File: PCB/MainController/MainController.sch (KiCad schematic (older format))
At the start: 48 parts, among them J1 5V, J2 PGM, J3 SERIAL, J4 I2C, J5 IO, J6 PWR, SW1 SW_Push, SW2 SW, SW3 SW, SW4 SW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

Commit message: pcb lcd
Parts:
- added J10: Jack-DC, Connect:BARREL_JACK, symbol Jack-DC
- J1: footprint Connectors_Molex:Molex_PicoBlade_53047-0410_04x1.25mm_Straight -> Pin_Headers:Pin_Header_Straight_1x04_Pitch2.54mm
- J7, J8, J9: renamed from J?; footprint MountingHole_2.7mm_M2.5_ISO14580_Pad -> Mounting_Holes:MountingHole_2.7mm_M2.5_ISO14580_Pad
- SW2, SW3, SW4, SW5: footprint Buttons_Switches_THT:SW_PUSH_6mm -> LCD:mySW_PUSH_6mm
- SW6: footprint Buttons_Switches_THT:KSA_Tactile_SPST -> LCD:myKSA_Tactile_SPST
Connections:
- net +3V3: now also J6.3 (Pin_3), J6.4 (Pin_4)
- net +5V: now also J10.1; no longer J6.3 (Pin_3), J6.4 (Pin_4)
- net GND: now also J10.2, J10.3
- net GPA0: now also J5.8 (Pin_8); no longer J5.1 (Pin_1)
- net GPA1: now also J5.7 (Pin_7); no longer J5.2 (Pin_2)
- net GPA2: now also J5.6 (Pin_6); no longer J5.3 (Pin_3)
- net GPA3: now also J5.5 (Pin_5); no longer J5.4 (Pin_4)
- net GPA4: now also J5.4 (Pin_4); no longer J5.5 (Pin_5)
- net GPA5: now also J5.3 (Pin_3); no longer J5.6 (Pin_6)
- net GPA6: now also J5.2 (Pin_2); no longer J5.7 (Pin_7)
- net GPA7: now also J5.1 (Pin_1); no longer J5.8 (Pin_8)
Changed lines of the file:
@@
 $EndDescr
-$Comp
-L dsPIC33EPXXXGP502 U3
-U 1 1 5B13F9B3
-P 4050 4550
-F 0 "U3" H 2900 6600 50  0000 L CNN
-F 1 "dsPIC33EPXXXGP502" H 2900 6500 50  0000 L CNN
-F 2 "Housings_SOIC:SOIC-28W_7.5x17.9mm_Pitch1.27mm" H 4900 6550 50  0000 C CIN
-F 3 "" H 3350 4150 60  0000 C CNN
-	1    4050 4550
-	1    0    0    -1
-$EndComp
-$Comp
-L NHD-0216K3Z U1
-U 1 1 5B140879
-P 2300 6100
-F 0 "U1" H 2850 6350 60  0000 C CNN
-F 1 "NHD-0216K3Z" H 2300 5850 60  0000 C CNN
-F 2 "LCD:WC1602A" H 2600 5800 60  0001 C CNN
-F 3 "" H 2600 5800 60  0001 C CNN
-	1    2300 6100
-	0    -1   1    0
-$EndComp
 $Comp
 L CP C4
@@
 F 0 "J1" H 2650 1250 50  0000 C CNN
 F 1 "5V" H 2650 750 50  0000 C CNN
-F 2 "Connectors_Molex:Molex_PicoBlade_53047-0410_04x1.25mm_Straight" H 2650 1050 50  0001 C CNN
+F 2 "Pin_Headers:Pin_Header_Straight_1x04_Pitch2.54mm" H 2650 1050 50  0001 C CNN
 F 3 "" H 2650 1050 50  0001 C CNN
 	1    2650 1050
@@
 F 0 "SW6" H 9800 5860 50  0000 C CNN
 F 1 "Rotary" H 9800 5340 50  0000 C CNN
-F 2 "Buttons_Switches_THT:KSA_Tactile_SPST" H 9700 5760 50  0001 C CNN
+F 2 "LCD:myKSA_Tactile_SPST" H 9700 5760 50  0001 C CNN
 F 3 "" H 9800 5860 50  0001 C CNN
 	1    9800 5600
@@
 	2150 1250 2150 1350
 Wire Wire Line
-	1850 900  2400 900
+	1650 900  2400 900
 Connection ~ 2150 900
 Connection ~ 2150 1300
@@
 	2400 1300 2400 1150
 Wire Wire Line
-	1850 1300 2400 1300
+	1650 1300 2400 1300
 Wire Wire Line
 	2400 1150 2450 1150
@@
 F 0 "SW2" H 8800 2800 50  0000 L CNN
 F 1 "SW" H 8500 2800 50  0000 C CNN
-F 2 "Buttons_Switches_THT:SW_PUSH_6mm" H 8650 2950 50  0001 C CNN
+F 2 "LCD:mySW_PUSH_6mm" H 8650 2950 50  0001 C CNN
 F 3 "" H 8650 2950 50  0001 C CNN
 	1    8650 2750
@@
 F 0 "SW3" H 8800 2900 50  0000 L CNN
 F 1 "SW" H 8500 2900 50  0000 C CNN
-F 2 "Buttons_Switches_THT:SW_PUSH_6mm" H 8650 3050 50  0001 C CNN
+F 2 "LCD:mySW_PUSH_6mm" H 8650 3050 50  0001 C CNN
 F 3 "" H 8650 3050 50  0001 C CNN
 	1    8650 2850
@@
 F 0 "SW4" H 8800 3000 50  0000 L CNN
 F 1 "SW" H 8500 3000 50  0000 C CNN
-F 2 "Buttons_Switches_THT:SW_PUSH_6mm" H 8650 3150 50  0001 C CNN
+F 2 "LCD:mySW_PUSH_6mm" H 8650 3150 50  0001 C CNN
 F 3 "" H 8650 3150 50  0001 C CNN
 	1    8650 2950
@@
 F 0 "SW5" H 8800 3100 50  0000 L CNN
 F 1 "SW" H 8500 3100 50  0000 C CNN
-F 2 "Buttons_Switches_THT:SW_PUSH_6mm" H 8650 3250 50  0001 C CNN
+F 2 "LCD:mySW_PUSH_6mm" H 8650 3250 50  0001 C CNN
 F 3 "" H 8650 3250 50  0001 C CNN
 	1    8650 3050
@@
 L Conn_01x08 J5
 U 1 1 5B158BF5
-P 8600 3950
-F 0 "J5" H 8600 4350 50  0000 C CNN
-F 1 "IO" H 8600 3450 50  0000 C CNN
-F 2 "Connectors_Molex:Molex_PicoBlade_53047-0810_08x1.25mm_Straight" H 8600 3950 50  0001 C CNN
-F 3 "" H 8600 3950 50  0001 C CNN
-	1    8600 3950
-	1    0    0    -1
+P 8600 4050
+F 0 "J5" H 8600 4450 50  0000 C CNN
+F 1 "IO" H 8600 3550 50  0000 C CNN
+F 2 "Connectors_Molex:Molex_PicoBlade_53047-0810_08x1.25mm_Straight" H 8600 4050 50  0001 C CNN
+F 3 "" H 8600 4050 50  0001 C CNN
+	1    8600 4050
+	1    0    0    1
 $EndComp
 Wire Wire Line
@@
 	-1   0    0    1
 $EndComp
-$Comp
-L +5V #PWR038
-U 1 1 5B15A6E4
-P 9250 3600
-F 0 "#PWR038" H 9250 3450 50  0001 C CNN
-F 1 "+5V" H 9250 3740 50  0000 C CNN
-F 2 "" H 9250 3600 50  0001 C CNN
-F 3 "" H 9250 3600 50  0001 C CNN
-	1    9250 3600
-	1    0    0    -1
-$EndComp
 Wire Wire Line
 	9100 3650 9250 3650
@@
 NoConn ~ 5350 2750
 $Comp
-L Conn_01x01 J?
+L Conn_01x01 J7
 U 1 1 5B158601
 P 9900 1450
-F 0 "J?" H 9900 1550 50  0000 C CNN
+F 0 "J7" H 9900 1550 50  0000 C CNN
 F 1 "MH" H 9900 1350 50  0000 C CNN
-F 2 "MountingHole_2.7mm_M2.5_ISO14580_Pad" H 9900 1450 50  0001 C CNN
+F 2 "Mounting_Holes:MountingHole_2.7mm_M2.5_ISO14580_Pad" H 9900 1450 50  0001 C CNN
 F 3 "" H 9900 1450 50  0001 C CNN
 	1    9900 1450
@@
 $EndComp
 $Comp
-L Conn_01x01 J?
+L Conn_01x01 J8
 U 1 1 5B1587EF
 P 9900 1750
-F 0 "J?" H 9900 1850 50  0000 C CNN
+F 0 "J8" H 9900 1850 50  0000 C CNN
 F 1 "MH" H 9900 1650 50  0000 C CNN
-F 2 "MountingHole_2.7mm_M2.5_ISO14580_Pad" H 9900 1750 50  0001 C CNN
+F 2 "Mounting_Holes:MountingHole_2.7mm_M2.5_ISO14580_Pad" H 9900 1750 50  0001 C CNN
 F 3 "" H 9900 1750 50  0001 C CNN
 	1    9900 1750
@@
 $EndComp
 $Comp
-L Conn_01x01 J?
+L Conn_01x01 J9
 U 1 1 5B158894
 P 9900 2000
-F 0 "J?" H 9900 2100 50  0000 C CNN
+F 0 "J9" H 9900 2100 50  0000 C CNN
 F 1 "MH" H 9900 1900 50  0000 C CNN
-F 2 "MountingHole_2.7mm_M2.5_ISO14580_Pad" H 9900 2000 50  0001 C CNN
+F 2 "Mounting_Holes:MountingHole_2.7mm_M2.5_ISO14580_Pad" H 9900 2000 50  0001 C CNN
 F 3 "" H 9900 2000 50  0001 C CNN
 	1    9900 2000
@@
 NoConn ~ 9700 1750
 NoConn ~ 9700 2000
+$Comp
+L dsPIC33EPXXXGP502 U3
+U 1 1 5B1FC9E1
+P 4050 4550
+F 0 "U3" H 2900 6600 50  0000 L CNN
+F 1 "dsPIC33EPXXXGP502" H 2900 6500 50  0000 L CNN
+F 2 "Housings_SOIC:SOIC-28W_7.5x17.9mm_Pitch1.27mm" H 4600 6500 50  0000 C CIN
+F 3 "" H 3350 4150 60  0000 C CNN
+	1    4050 4550
+	1    0    0    -1
+$EndComp
+$Comp
+L NHD-0216K3Z U1
+U 1 1 5B1FCCB6
+P 2300 6100
+F 0 "U1" H 2850 6350 60  0000 C CNN
+F 1 "NHD-0216K3Z" H 2300 5850 60  0000 C CNN
+F 2 "LCD:WC1602A" H 2600 5800 60  0001 C CNN
+F 3 "" H 2600 5800 60  0001 C CNN
+	1    2300 6100
+	0    -1   1    0
+$EndComp
+$Comp
+L Jack-DC J10
+U 1 1 5B1FEC81
+P 1150 1100
+F 0 "J10" H 1150 1310 50  0000 C CNN
+F 1 "Jack-DC" H 1150 925 50  0000 C CNN
+F 2 "Connect:BARREL_JACK" H 1200 1060 50  0001 C CNN
+F 3 "" H 1200 1060 50  0001 C CNN
+	1    1150 1100
+	1    0    0    -1
+$EndComp
+Wire Wire Line
+	1450 1200 1650 1200
+Wire Wire Line
+	1650 1100 1650 1300
+Connection ~ 1850 1300
+Wire Wire Line
+	1450 1000 1650 1000
+Wire Wire Line
+	1650 1000 1650 900
+Connection ~ 1850 900
+Wire Wire Line
+	1450 1100 1650 1100
+Connection ~ 1650 1200
+$Comp
+L +3.3V #PWR?
+U 1 1 5B200FD1
+P 9250 3600
+F 0 "#PWR?" H 9250 3450 50  0001 C CNN
+F 1 "+3.3V" H 9250 3740 50  0000 C CNN
+F 2 "" H 9250 3600 50  0001 C CNN
+F 3 "" H 9250 3600 50  0001 C CNN
+	1    9250 3600
+	1    0    0    -1
+$EndComp
 $EndSCHEMATC

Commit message: pcb lcd
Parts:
- added D5, D6, D7: LED, LEDs:LED_0603_HandSoldering, symbol LED
- added R14, R15, R16: 2.87k, Resistors_SMD:R_0603_HandSoldering, symbol R
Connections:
- net GND: now also D5.1 (K), D6.1 (K), D7.1 (K)
- net at U3.2 (AN0/OA2OUT/RA0): now also R14.2
- net at U3.3 (AN1/C2IN1+/RA1): now also R15.2
- net at U3.4 (PGED3/V_REF_-/AN2/C2IN1-/SS1/RPI32/CTED2/RB0): now also R16.2
- new net: D5.2 (A), R16.1
- new net: D6.2 (A), R15.1
- new net: D7.2 (A), R14.1
- no-connect marks 13 -> 10
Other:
- moved on the sheet: C9, J5, J6, J9, SW2, SW3, SW4, SW5, U4

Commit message: create main pcb
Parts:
- SW6: footprint LCD:myKSA_Tactile_SPST -> Rotary-Encoders:ALPS_STEC12E08

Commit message: clean up main controller pcb
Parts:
- added J11, J12: MH, Mounting_Holes:MountingHole_2.7mm_M2.5_ISO14580_Pad, symbol Conn_01x01
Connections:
- no-connect marks 10 -> 12
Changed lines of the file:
@@
 LIBS:contrib
 LIBS:valves
+LIBS:MyLib
 LIBS:MainController-cache
 EELAYER 25 0
@@
 Wire Wire Line
 	7000 3950 7000 4050
+$Comp
+L Conn_01x01 J12
+U 1 1 5B22365B
+P 10850 1700
+F 0 "J12" H 10850 1800 50  0000 C CNN
+F 1 "MH" H 10850 1600 50  0000 C CNN
+F 2 "Mounting_Holes:MountingHole_2.7mm_M2.5_ISO14580_Pad" H 10850 1700 50  0001 C CNN
+F 3 "" H 10850 1700 50  0001 C CNN
+	1    10850 1700
+	1    0    0    -1
+$EndComp
+$Comp
+L Conn_01x01 J11
+U 1 1 5B223739
+P 10850 1400
+F 0 "J11" H 10850 1500 50  0000 C CNN
+F 1 "MH" H 10850 1300 50  0000 C CNN
+F 2 "Mounting_Holes:MountingHole_2.7mm_M2.5_ISO14580_Pad" H 10850 1400 50  0001 C CNN
+F 3 "" H 10850 1400 50  0001 C CNN
+	1    10850 1400
+	1    0    0    -1
+$EndComp
+NoConn ~ 10650 1700
+NoConn ~ 10650 1400
 $EndSCHEMATC

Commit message: opening mplab
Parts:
- added J13: PIC_IO, Pin_Headers:Pin_Header_Straight_1x05_Pitch2.54mm, symbol Conn_01x05
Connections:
- net +3V3: now also J13.1 (Pin_1)
- net GND: now also J13.2 (Pin_2)
- net RA0: now reaches R14.2, U3.2 (AN0/OA2OUT/RA0)
- net RA0: now also J13.3 (Pin_3)
- net RA1: now reaches R15.2, U3.3 (AN1/C2IN1+/RA1)
- net RA1: now also J13.4 (Pin_4)
- net RB0: now reaches R16.2, U3.4 (PGED3/V_REF_-/AN2/C2IN1-/SS1/RPI32/CTED2/RB0)
- net RB0: now also J13.5 (Pin_5)
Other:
- moved on the sheet: J11, J12, J7, J8, J9
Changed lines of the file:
@@
 L Conn_01x01 J7
 U 1 1 5B158601
-P 9900 1450
-F 0 "J7" H 9900 1550 50  0000 C CNN
-F 1 "MH" H 9900 1350 50  0000 C CNN
-F 2 "Mounting_Holes:MountingHole_2.7mm_M2.5_ISO14580_Pad" H 9900 1450 50  0001 C CNN
-F 3 "" H 9900 1450 50  0001 C CNN
-	1    9900 1450
+P 9950 1750
+F 0 "J7" H 9950 1850 50  0000 C CNN
+F 1 "MH" H 9950 1650 50  0000 C CNN
+F 2 "Mounting_Holes:MountingHole_2.7mm_M2.5_ISO14580_Pad" H 9950 1750 50  0001 C CNN
+F 3 "" H 9950 1750 50  0001 C CNN
+	1    9950 1750
 	1    0    0    -1
 $EndComp
@@
 L Conn_01x01 J8
 U 1 1 5B1587EF
-P 9900 1750
-F 0 "J8" H 9900 1850 50  0000 C CNN
-F 1 "MH" H 9900 1650 50  0000 C CNN
-F 2 "Mounting_Holes:MountingHole_2.7mm_M2.5_ISO14580_Pad" H 9900 1750 50  0001 C CNN
-F 3 "" H 9900 1750 50  0001 C CNN
-	1    9900 1750
+P 9950 2050
+F 0 "J8" H 9950 2150 50  0000 C CNN
+F 1 "MH" H 9950 1950 50  0000 C CNN
+F 2 "Mounting_Holes:MountingHole_2.7mm_M2.5_ISO14580_Pad" H 9950 2050 50  0001 C CNN
+F 3 "" H 9950 2050 50  0001 C CNN
+	1    9950 2050
 	1    0    0    -1
 $EndComp
@@
 L Conn_01x01 J9
 U 1 1 5B158894
-P 10850 2000
-F 0 "J9" H 10850 2100 50  0000 C CNN
-F 1 "MH" H 10850 1900 50  0000 C CNN
-F 2 "Mounting_Holes:MountingHole_2.7mm_M2.5_ISO14580_Pad" H 10850 2000 50  0001 C CNN
-F 3 "" H 10850 2000 50  0001 C CNN
-	1    10850 2000
-	1    0    0    -1
-$EndComp
-NoConn ~ 9700 1450
-NoConn ~ 9700 1750
-NoConn ~ 10650 2000
+P 10900 2300
+F 0 "J9" H 10900 2400 50  0000 C CNN
+F 1 "MH" H 10900 2200 50  0000 C CNN
+F 2 "Mounting_Holes:MountingHole_2.7mm_M2.5_ISO14580_Pad" H 10900 2300 50  0001 C CNN
+F 3 "" H 10900 2300 50  0001 C CNN
+	1    10900 2300
+	1    0    0    -1
+$EndComp
+NoConn ~ 9750 1750
+NoConn ~ 9750 2050
+NoConn ~ 10700 2300
 $Comp
 L dsPIC33EPXXXGP502 U3
@@
 L Conn_01x01 J12
 U 1 1 5B22365B
-P 10850 1700
-F 0 "J12" H 10850 1800 50  0000 C CNN
-F 1 "MH" H 10850 1600 50  0000 C CNN
-F 2 "Mounting_Holes:MountingHole_2.7mm_M2.5_ISO14580_Pad" H 10850 1700 50  0001 C CNN
-F 3 "" H 10850 1700 50  0001 C CNN
-	1    10850 1700
+P 10900 2000
+F 0 "J12" H 10900 2100 50  0000 C CNN
+F 1 "MH" H 10900 1900 50  0000 C CNN
+F 2 "Mounting_Holes:MountingHole_2.7mm_M2.5_ISO14580_Pad" H 10900 2000 50  0001 C CNN
+F 3 "" H 10900 2000 50  0001 C CNN
+	1    10900 2000
 	1    0    0    -1
 $EndComp
@@
 L Conn_01x01 J11
 U 1 1 5B223739
-P 10850 1400
-F 0 "J11" H 10850 1500 50  0000 C CNN
-F 1 "MH" H 10850 1300 50  0000 C CNN
-F 2 "Mounting_Holes:MountingHole_2.7mm_M2.5_ISO14580_Pad" H 10850 1400 50  0001 C CNN
-F 3 "" H 10850 1400 50  0001 C CNN
-	1    10850 1400
-	1    0    0    -1
-$EndComp
-NoConn ~ 10650 1700
-NoConn ~ 10650 1400
+P 10900 1700
+F 0 "J11" H 10900 1800 50  0000 C CNN
+F 1 "MH" H 10900 1600 50  0000 C CNN
+F 2 "Mounting_Holes:MountingHole_2.7mm_M2.5_ISO14580_Pad" H 10900 1700 50  0001 C CNN
+F 3 "" H 10900 1700 50  0001 C CNN
+	1    10900 1700
+	1    0    0    -1
+$EndComp
+NoConn ~ 10700 2000
+NoConn ~ 10700 1700
+$Comp
+L Conn_01x05 J13
+U 1 1 5B349CC6
+P 9600 1150
+F 0 "J13" H 9600 1450 50  0000 C CNN
+F 1 "PIC_IO" V 9700 1150 50  0000 C CNN
+F 2 "Pin_Headers:Pin_Header_Straight_1x05_Pitch2.54mm" H 9600 1150 50  0001 C CNN
+F 3 "" H 9600 1150 50  0001 C CNN
+	1    9600 1150
+	-1   0    0    -1
+$EndComp
+Wire Wire Line
+	10250 1100 10250 1050
+Wire Wire Line
+	10250 1050 9800 1050
+Text Label 5450 2750 0    60   ~ 0
+RA0
+Text Label 5450 2850 0    60   ~ 0
+RA1
+Text Label 5450 3350 0    60   ~ 0
+RB0
+Text Label 9900 1150 0    60   ~ 0
+RA0
+Text Label 9900 1250 0    60   ~ 0
+RA1
+Text Label 9900 1350 0    60   ~ 0
+RB0
+Wire Wire Line
+	9800 1150 9900 1150
+Wire Wire Line
+	9800 1250 9900 1250
+Wire Wire Line
+	9800 1350 9900 1350
+$Comp
+L GND #PWR045
+U 1 1 5B34A257
+P 10250 1100
+F 0 "#PWR045" H 10250 850 50  0001 C CNN
+F 1 "GND" H 10250 950 50  0000 C CNN
+F 2 "" H 10250 1100 50  0001 C CNN
+F 3 "" H 10250 1100 50  0001 C CNN
+	1    10250 1100
+	1    0    0    -1
+$EndComp
+Wire Wire Line
+	10250 950  10250 900
+$Comp
+L +3.3V #PWR044
+U 1 1 5B34A19E
+P 10250 900
+F 0 "#PWR044" H 10250 750 50  0001 C CNN
+F 1 "+3.3V" H 10250 1040 50  0000 C CNN
+F 2 "" H 10250 900 50  0001 C CNN
+F 3 "" H 10250 900 50  0001 C CNN
+	1    10250 900
+	1    0    0    -1
+$EndComp
+Wire Wire Line
+	9800 950  10250 950
 $EndSCHEMATC

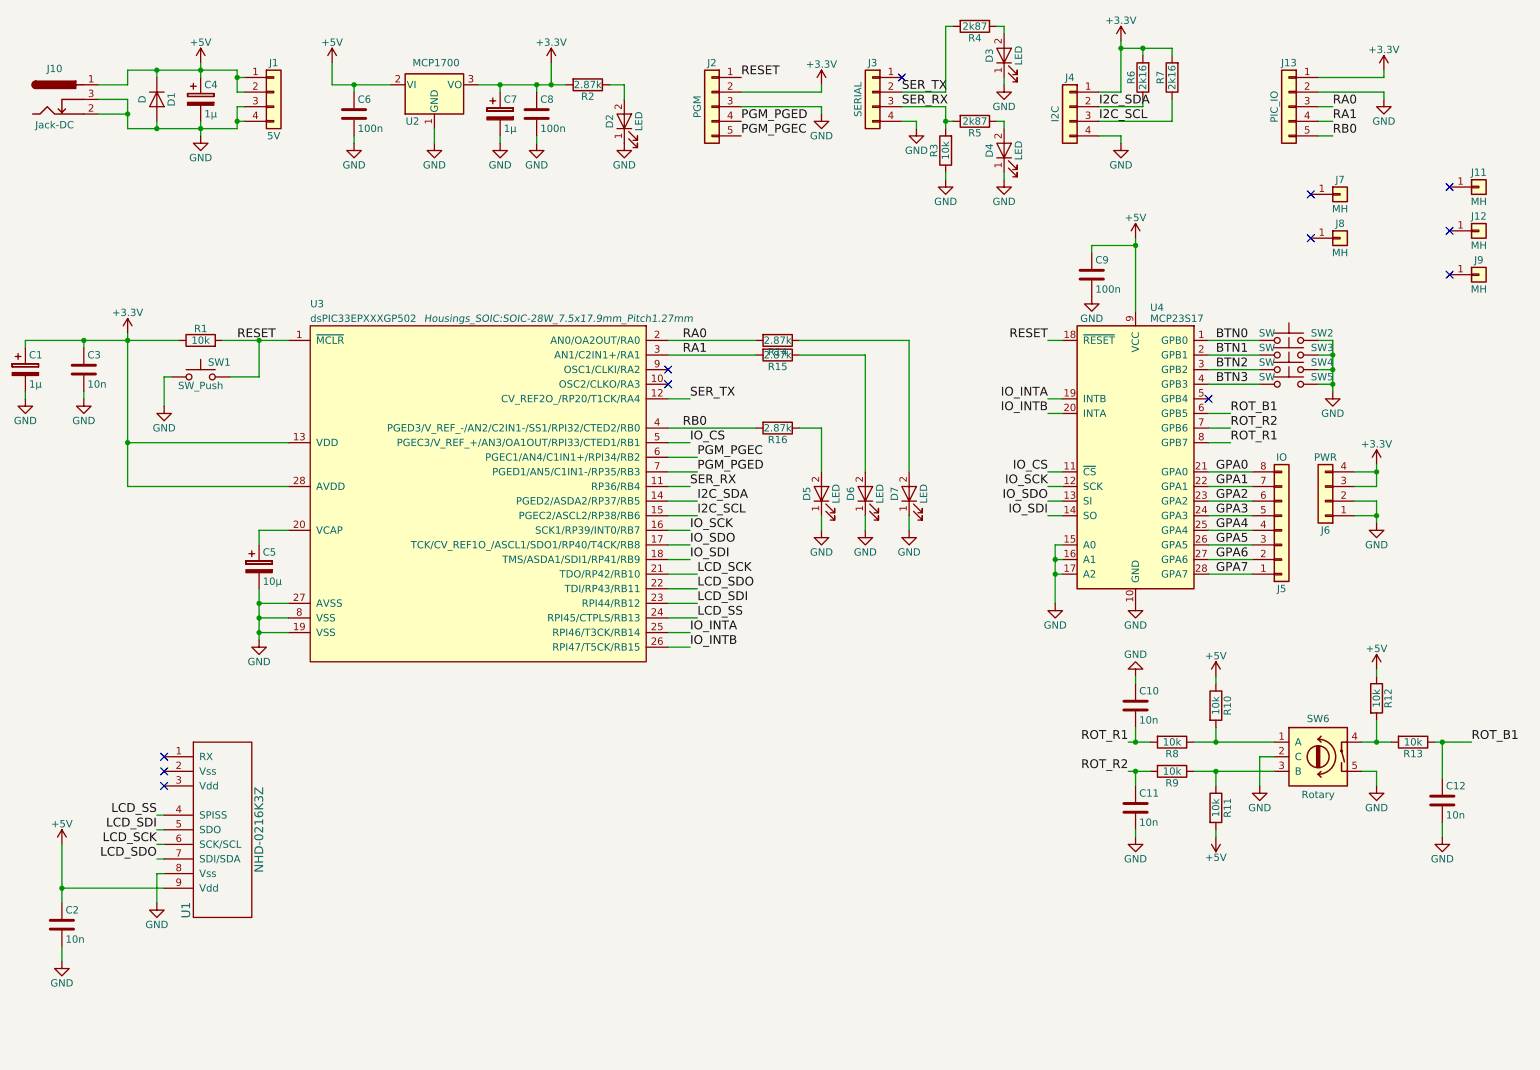
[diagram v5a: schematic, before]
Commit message: updated pcb for MPC23S power supply error
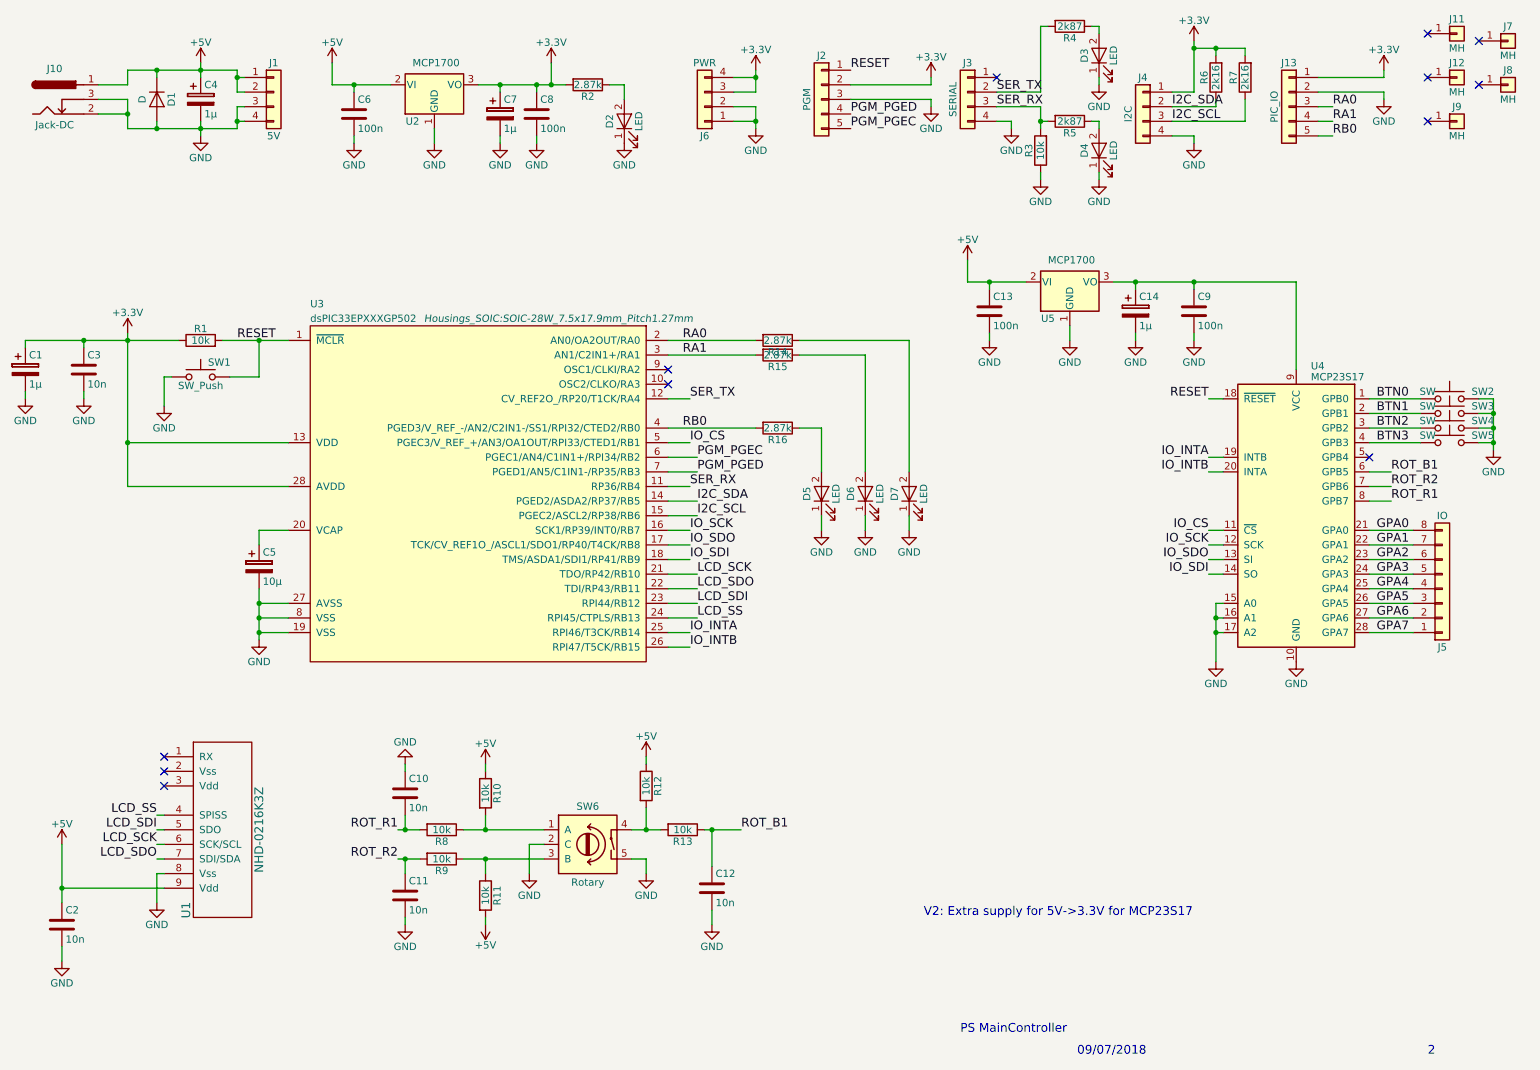
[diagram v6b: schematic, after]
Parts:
- added C13: 100n, Capacitors_SMD:C_0603_HandSoldering, symbol C
- added C14: 1µ, Capacitors_Tantalum_SMD:CP_Tantalum_Case-A_EIA-3216-18_Reflow, symbol CP
- added U5: MCP1700, TO_SOT_Packages_THT:TO-92_Inline_Narrow_Oval, symbol MCP1700-3302E_TO92
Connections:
- net +5V: now also C13.1, U5.2 (VI); no longer C9.1, U4.9 (VCC)
- net GND: now also C13.2, C14.2, U5.1 (GND)
- new net: C14.1, C9.1, U4.9 (VCC), U5.3 (VO)
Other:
- note added: "09/07/2018"
- note added: "2"
- note added: "PS MainController"
- note added: "V2: Extra supply for 5V->3.3V for MCP23S17"
- moved on the sheet: C10, C11, C12, C9, D3, D4, J11, J12, J2, J3, J4, J5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

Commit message: added description and windows builds
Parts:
- C1, C14, C4, C5, C7: symbol CP -> Device:CP
- C10, C11, C12, C13, C2, C3, C6, C8, C9: symbol C -> Device:C
- D1: symbol D -> Device:D
- D2, D3, D4, D5, D6, D7: symbol LED -> Device:LED
- J1, J3, J4, J6: symbol Conn_01x04 -> MainController-rescue:Conn_01x04
- J10: symbol Jack-DC -> MainController-rescue:Jack-DC
- J11, J12, J7, J8, J9: symbol Conn_01x01 -> MainController-rescue:Conn_01x01
- J13, J2: symbol Conn_01x05 -> MainController-rescue:Conn_01x05
- J5: symbol Conn_01x08 -> MainController-rescue:Conn_01x08
- R1, R10, R11, R12, R13, R14, R15, R16, R2, R3, R4, R5, R6, R7, R8, R9: symbol R -> Device:R
- SW1, SW2, SW3, SW4, SW5: symbol SW_Push -> MainController-rescue:SW_Push
- SW6: symbol Rotary_Encoder_Switch -> MainController-rescue:Rotary_Encoder_Switch
- U1: symbol NHD-0216K3Z -> MainController-rescue:NHD-0216K3Z
- U2, U5: symbol MCP1700-3302E_TO92 -> MainController-rescue:MCP1700-3302E_TO92
- U3: symbol dsPIC33EPXXXGP502 -> MainController-rescue:dsPIC33EPXXXGP502
- U4: symbol MCP23S17 -> MainController-rescue:MCP23S17
